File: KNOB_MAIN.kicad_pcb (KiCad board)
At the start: 2 copper layers, 100 x 30 mm, 21 parts, among them J1 HRO_TYPE-C-31-M-12, SW1 PEC11R-4220F-S0024, U1 AMS1117-3.3, U2 ESP32-C3-MINI-1

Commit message: Output gerber
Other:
- board text added: "KNOB_MAIN V1.0 by XiNGRZ"
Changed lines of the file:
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@@
   (general
     (thickness 1.2)
-    (drawings 45)
+    (drawings 46)
     (tracks 291)
     (zones 0)
@@
     )
   )
+  (gr_text "KNOB_MAIN V1.0 by XiNGRZ" (at 192 98) (layer F.SilkS)
+    (effects (font (size 0.8 0.8) (thickness 0.12)) (justify right))
+  )
   (dimension 10 (width 0.15) (layer Dwgs.User)

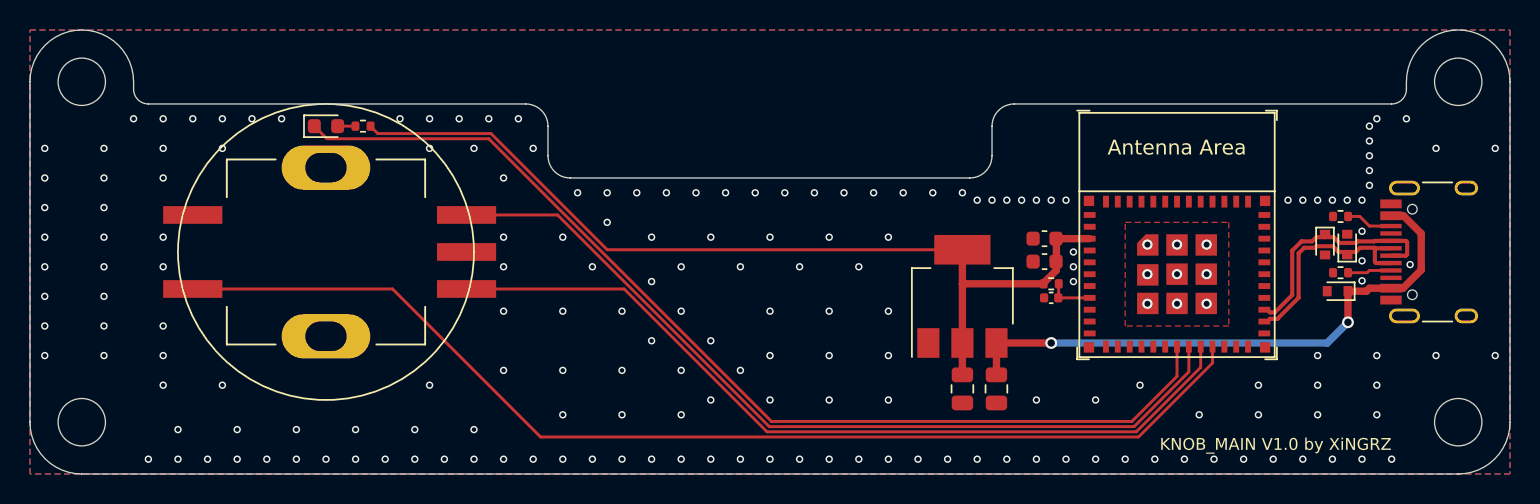
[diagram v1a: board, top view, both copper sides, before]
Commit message: Use LP2992AIM5X-3.3 LDO and adjust layout
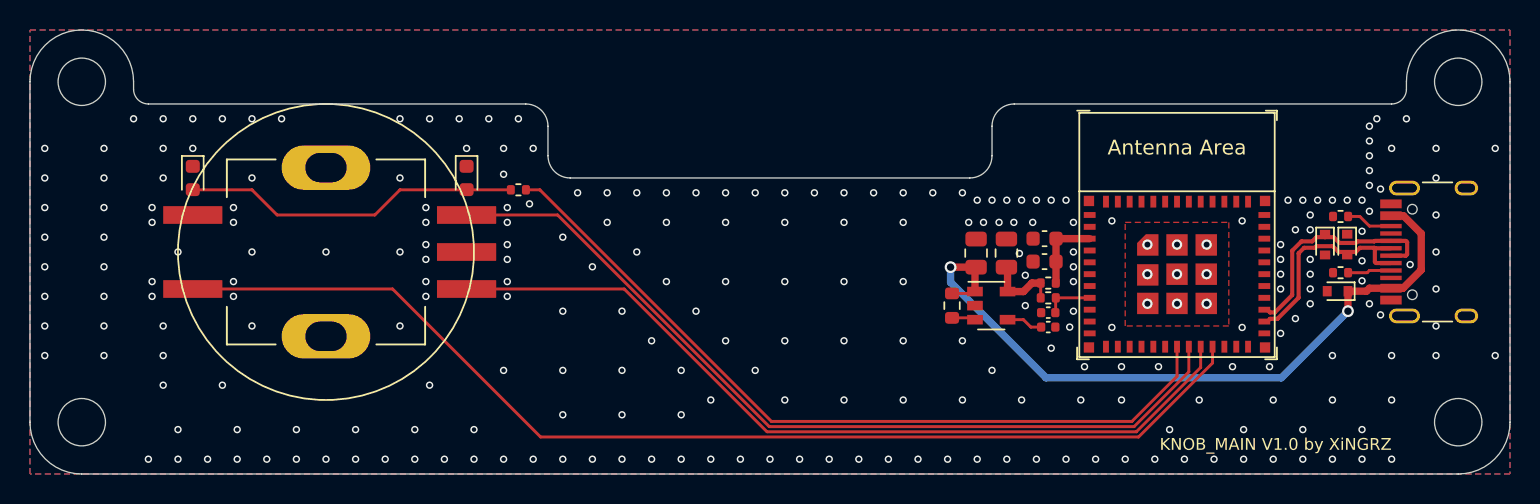
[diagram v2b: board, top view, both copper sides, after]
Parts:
- added C6: 10nF, Capacitor_SMD:C_0402_1005Metric, F.Cu at (168.8, 90.1)
- added D5: BLUE, LED_SMD:LED_0603_1608Metric, F.Cu at (111.0, 80.0)
- added R5: 0, Resistor_SMD:R_0603_1608Metric, F.Cu at (162.3, 88.6)
- added R6: 220, Resistor_SMD:R_0402_1005Metric, F.Cu at (133.0, 80.8)
- D4: value STATUS -> BLUE
- R4: value 2K -> 0
- U1: value AMS1117-3.3 -> LP2992AIM5X-3.3; footprint Package_TO_SOT_SMD:SOT-223-3_TabPin2 -> Package_TO_SOT_SMD:SOT-23-5
- moved R4 47.5 mm to (168.8, 87.1)
- moved D4 10.1 mm to (129.5, 80.0), turned to 270 degrees
- moved C2 9.65 mm to (166.0, 85.1), turned to 90 degrees
- moved C1 9.28 mm to (163.9, 85.1), turned to 90 degrees
- moved U1 2.05 mm to (164.9, 88.6), turned to 0 degrees
- moved C3 1.02 mm to (168.8, 89.1)
- moved R3 0.97 mm to (168.8, 88.1)
- turned D2 to 270 degrees
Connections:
- net /VOL_DN renamed /ROTARY_B
- net /VOL_UP renamed /ROTARY_A
- C4 pad 1: +3V3 -> Net-(C4-Pad1)
- C5 pad 1: +3V3 -> Net-(C4-Pad1)
- D2 pad 1: /D- -> GND
- D2 pad 2: GND -> /D-
- D4 pad 1: /STATUS -> GND
- J1 pad S1: GND -> Net-(J1-PadS1)
- R4 pad 1: Net-(D4-Pad2) -> +3V3
- R4 pad 2: +3V3 -> Net-(C4-Pad1)
- U1 pad 1: GND -> +5V
- U1 pad 2: +3V3 -> GND
- U1 pad 3: +5V -> Net-(R5-Pad1)
- U2 pad 3: +3V3 -> Net-(C4-Pad1)
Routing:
- net +3V3: track 63.0 -> 5.12 mm
- net Net-(D4-Pad2): track 1.21 -> 22.9 mm
- net /STATUS: track 69.8 -> 53.7 mm
- net +5V: track 39.1 -> 49.2 mm
- net Net-(C4-Pad1): track 0.00 -> 5.25 mm
- net Net-(C6-Pad1): track 0.00 -> 2.48 mm
- net Net-(R5-Pad1): track 0.00 -> 1.55 mm
- net GND: vias 195 -> 265
